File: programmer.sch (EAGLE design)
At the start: 16 parts, among them U1 ATMEGA8U2AU, Y1 16 MHz

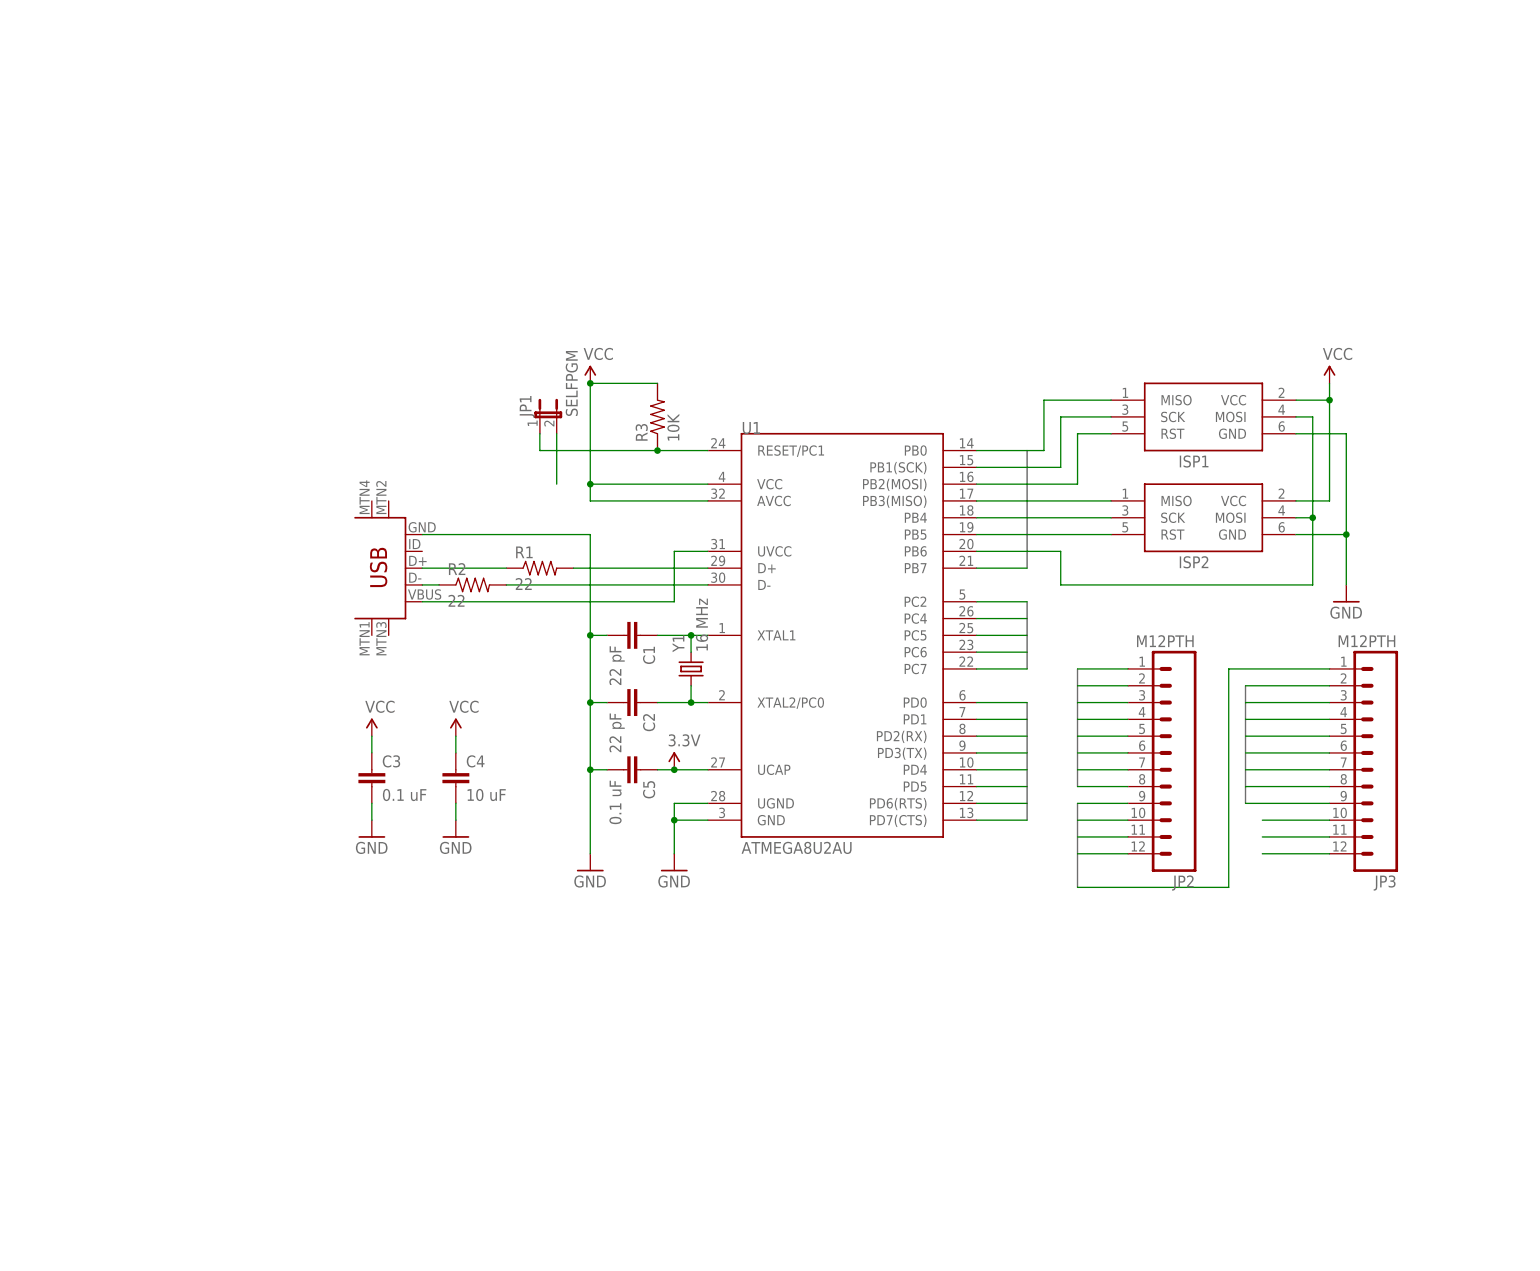
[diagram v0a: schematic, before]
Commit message: Angled 6-pin ISP.
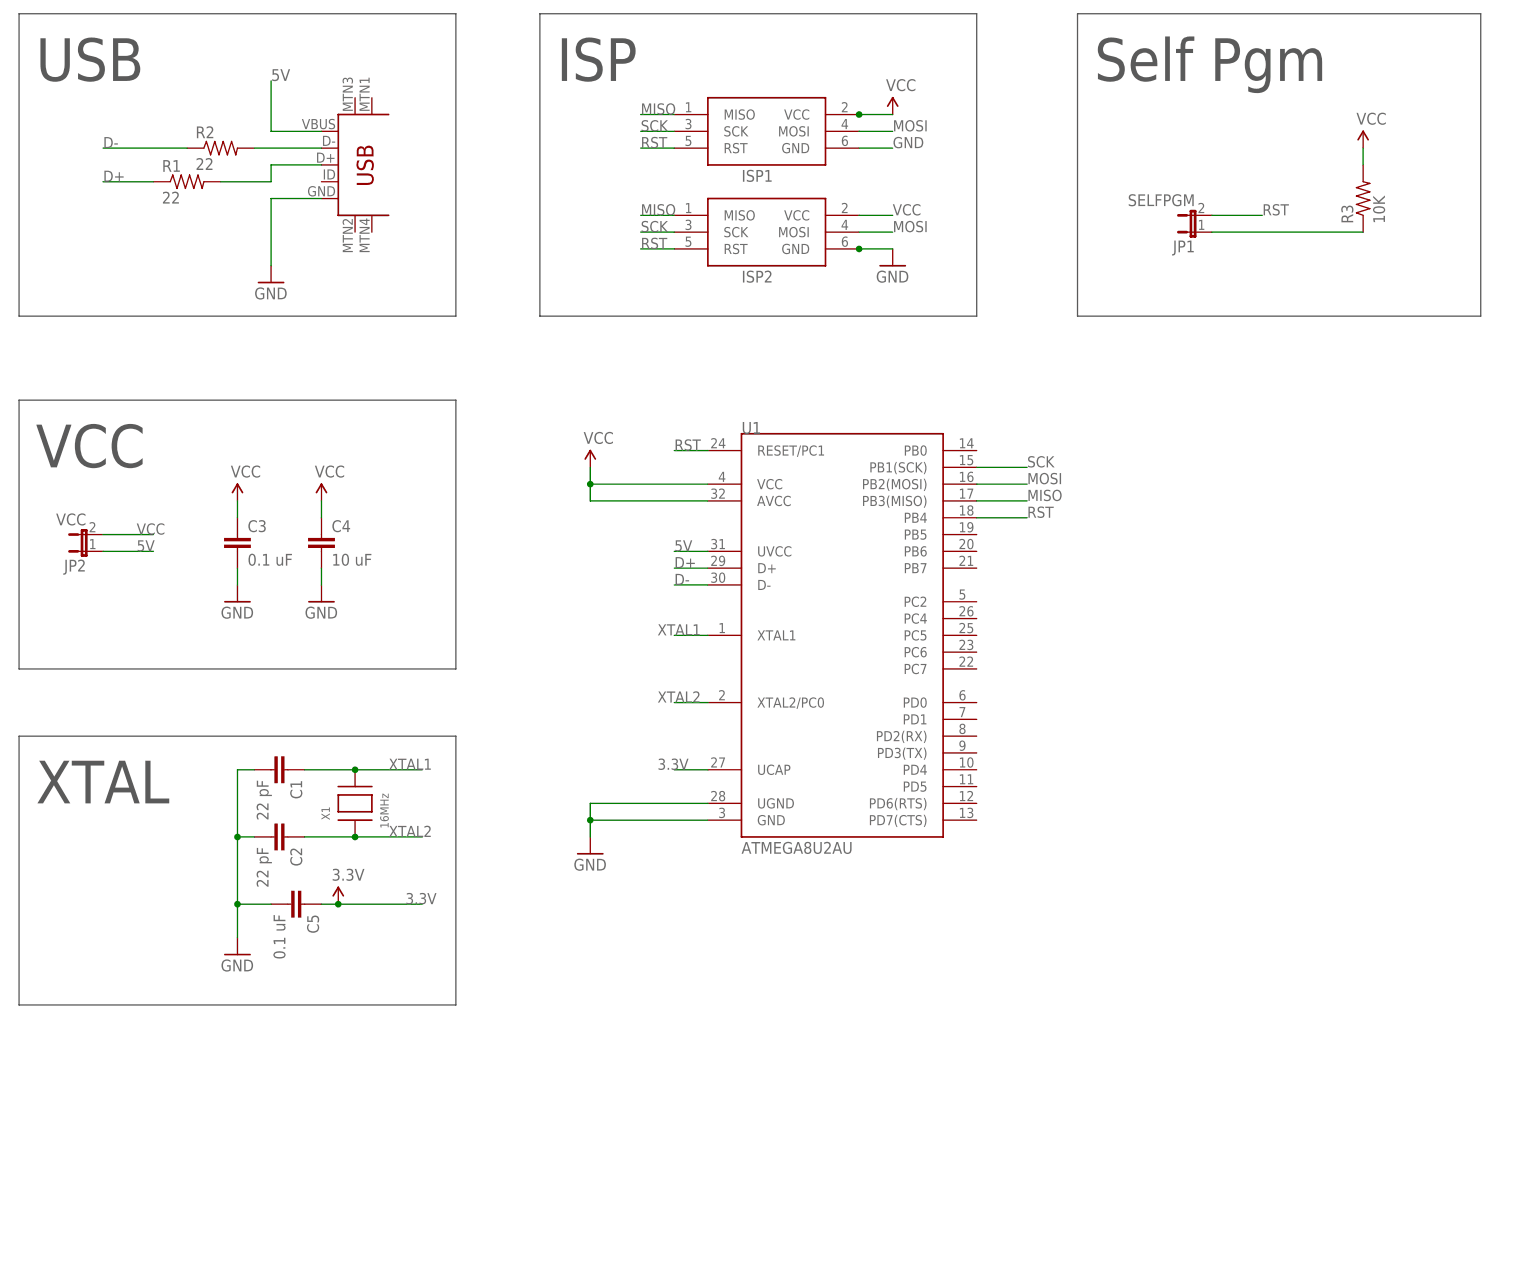
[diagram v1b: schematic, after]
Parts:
- removed JP3: M12PTH, SparkFun:M12PTH
- removed Y1: 16 MHz, SparkFun:CRYSTAL10.5X4.8
- added X1: 16MHz, adafruit:XTALNX8045
- JP2: value M12PTH -> VCC; device SparkFun:M12PTH -> SparkFun:JUMPER-2PTH
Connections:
- removed net D_MINUS: R2.1, U$1.D-
- removed net D_MINUS_MCU: R2.2, U1.D-
- removed net D_PLUS: R1.1, U$1.D+
- removed net D_PLUS_MCU: R1.2, U1.D+
- removed net N$5: U$1.VBUS, U1.UVCC
- removed net PB0: JP2.1, U1.PB0
- removed net PB1: ISP1.SCK, ISP2.SCK, JP2.2, U1.PB1(SCK)
- removed net PB2: ISP1.MOSI, ISP2.MOSI, JP2.3, U1.PB2(MOSI)
- removed net PB3: ISP1.MISO, ISP2.MISO, JP2.4, U1.PB3(MISO)
- removed net PB4: ISP1.RST, ISP2.RST, JP1.2, JP2.5, U1.PB4
- removed net PB5: JP2.6, U1.PB5
- removed net PB6: JP2.7, U1.PB6
- removed net PB7: JP2.8, U1.PB7
- removed net PC2: JP2.9, U1.PC2
- removed net PC4: JP2.10, U1.PC4
- removed net PC5: JP2.11, U1.PC5
- removed net PC6: JP2.12, U1.PC6
- removed net PC7: JP3.1, U1.PC7
- removed net PD0: JP3.2, U1.PD0
- removed net PD1: JP3.3, U1.PD1
- removed net PD2: JP3.4, U1.PD2(RX)
- removed net PD3: JP3.5, U1.PD3(TX)
- removed net PD4: JP3.6, U1.PD4
- removed net PD5: JP3.7, U1.PD5
- removed net PD6: JP3.8, U1.PD6(RTS)
- removed net PD7: JP3.9, U1.PD7(CTS)
- new net 5V: JP2.1, U$1.VBUS, U1.UVCC
- new net D+: R1.1, U1.D+
- new net D+RAW: R1.2, U$1.D+
- new net D-: R2.1, U1.D-
- new net MISO: ISP1.MISO, ISP2.MISO, U1.PB3(MISO)
- new net MOSI: ISP1.MOSI, ISP2.MOSI, U1.PB2(MOSI)
- new net N$2: R2.2, U$1.D-
- new net RST: ISP1.RST, ISP2.RST, JP1.2, U1.PB4, U1.RESET/PC1
- new net SCK: ISP1.SCK, ISP2.SCK, U1.PB1(SCK)
- net 3.3V: no longer JP3.10
- net GND: no longer JP3.12
- net RST_JP1: no longer U1.RESET/PC1
- net VCC: now also JP2.2; no longer JP3.11
- net XTAL1: now also X1.P$2; no longer Y1.2
- net XTAL2: now also X1.P$1; no longer Y1.1
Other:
- note added: "ISP"
- note added: "Self Pgm"
- note added: "USB"
- note added: "VCC"
- note added: "XTAL"
- moved on the sheet: C1, C2, C3, C4, C5, ISP1, ISP2, JP1, R1, R2, R3

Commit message: Blinkenlights.
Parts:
- added LED1, LED2: (no value), adafruit:LEDSMT1206
- added R4, R5: 1K, SparkFun:RESISTOR0805-RES
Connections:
- new net LED_ACTIVE: LED2.C, U1.PD1
- new net LED_WRITE: LED1.C, U1.PD0
- new net N$1: LED2.A, R5.1
- new net N$3: LED1.A, R4.1
- net VCC: now also R4.2, R5.2
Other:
- note added: "LED"
- moved on the sheet: U1

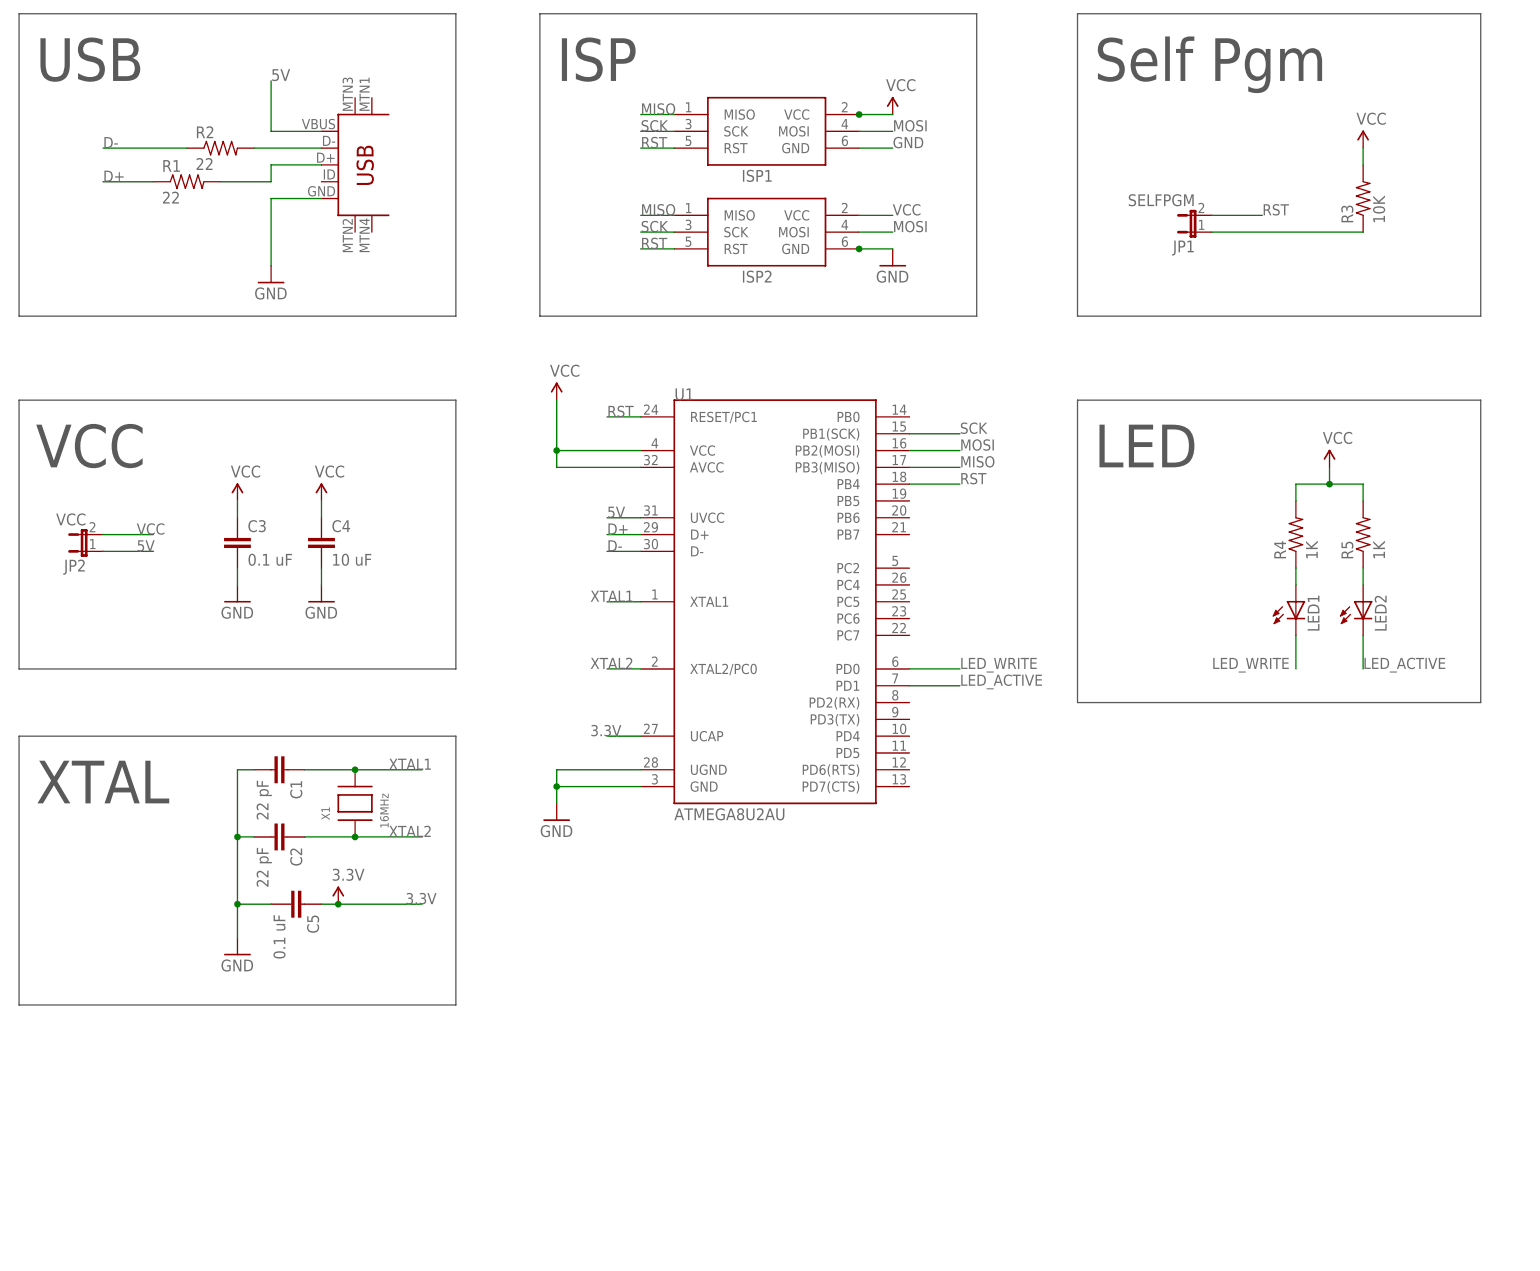
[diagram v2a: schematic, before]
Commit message: More work on layout. SJ1. Polarized 10uF cap. Fixed ISP2 orientation.
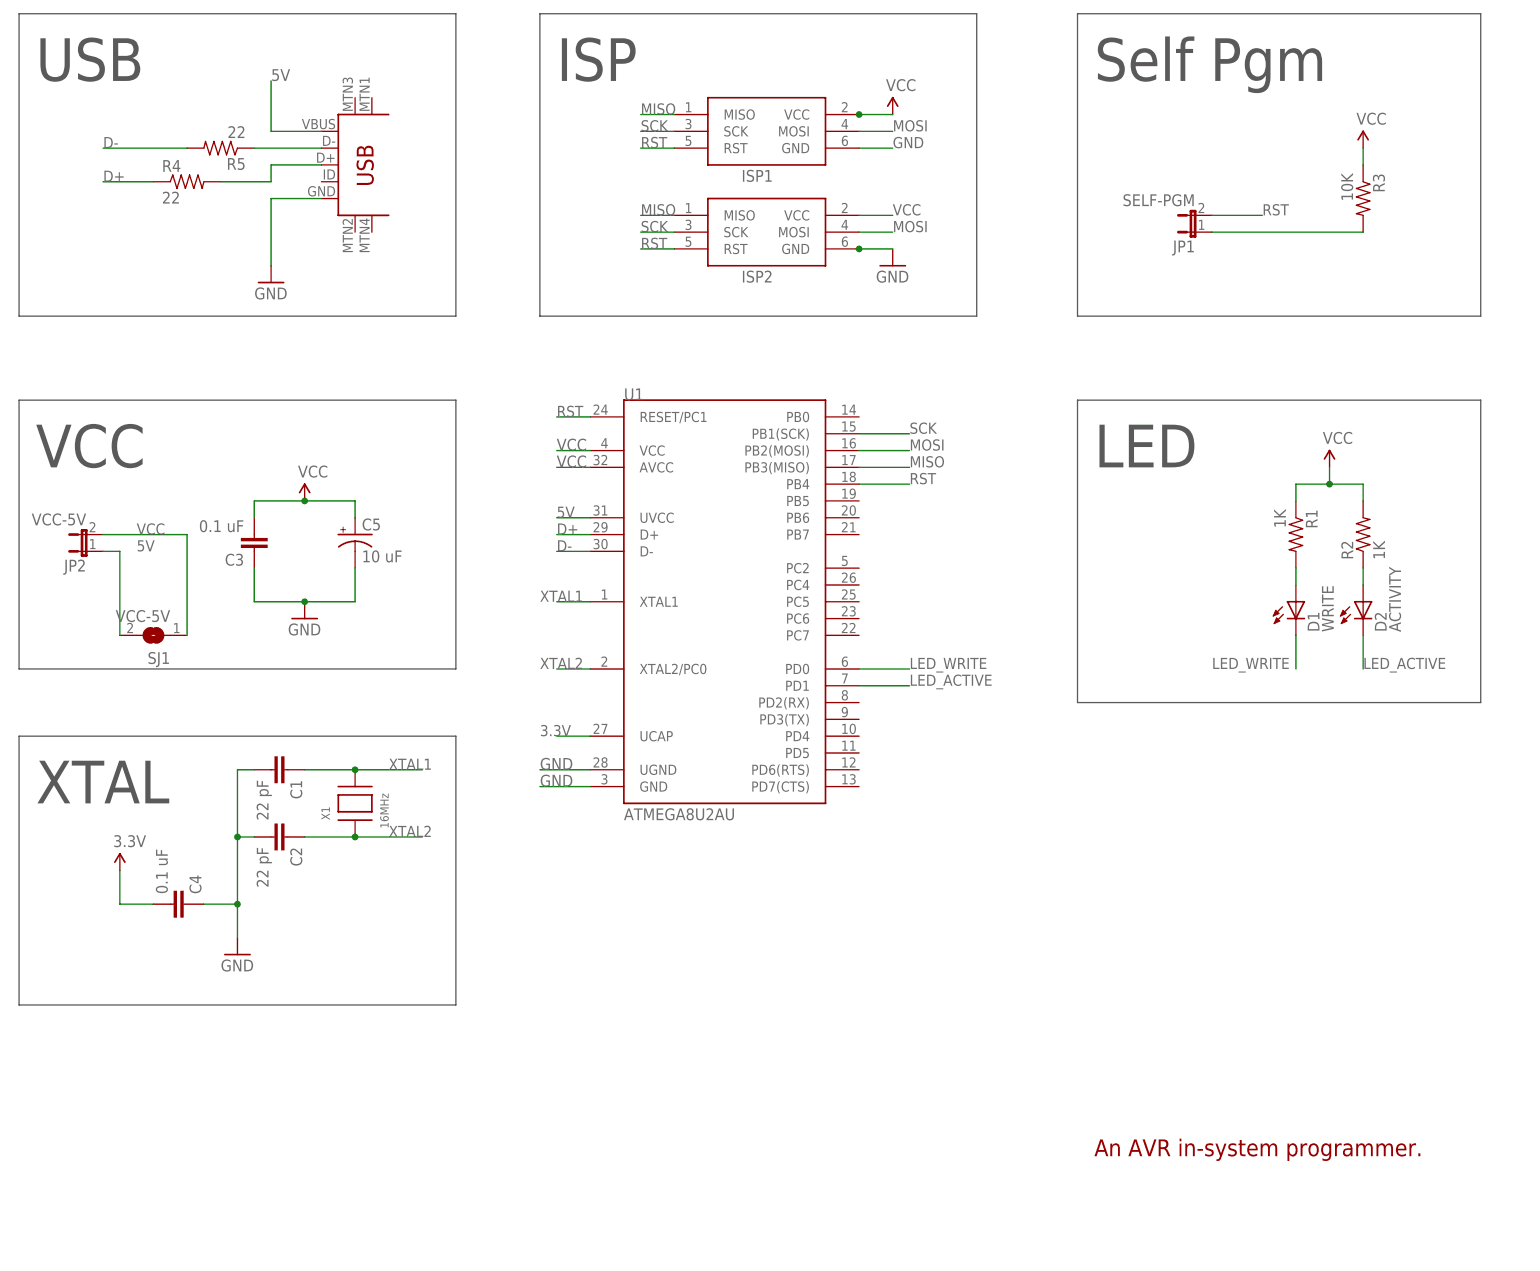
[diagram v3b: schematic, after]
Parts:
- added SJ1: VCC-5V, jumper:SJ
- C4: value 10 uF -> 0.1 uF
- C5: value 0.1 uF -> 10 uF; device SparkFun:CAP0805 -> SparkFun:CAP_POL1206
- D1: value (none) -> WRITE
- D2: value (none) -> ACTIVITY
- JP1: value SELFPGM -> SELF-PGM
- JP2: value VCC -> VCC-5V
- R1, R2: value 22 -> 1K
- R4, R5: value 1K -> 22
- renumbered LED1 to D1, LED2 to D2, U$1 to USB
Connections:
- net 3.3V: now also C4.2; no longer C5.1
- net 5V: now also SJ1.2
- net D+: now also R4.1; no longer R1.1
- net D+RAW: now also R4.2; no longer R1.2
- net D-: now also R5.2; no longer R2.1
- net GND: now also C3.1, C4.1, C5.-; no longer C3.2, C4.2, C5.2
- net N$1: now also R2.1; no longer R5.1
- net N$2: now also R5.1; no longer R2.2
- net N$3: now also R1.2; no longer R4.1
- net RST_JP1: now also R3.2; no longer R3.1
- net VCC: now also C3.2, C5.+, R1.1, R2.2, R3.1, SJ1.1; no longer C3.1, C4.1, R3.2, R4.2, R5.2
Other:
- note added: "An AVR in-system programmer."
- moved on the sheet: C3, C4, R1, R2, R3, R4, R5, U1

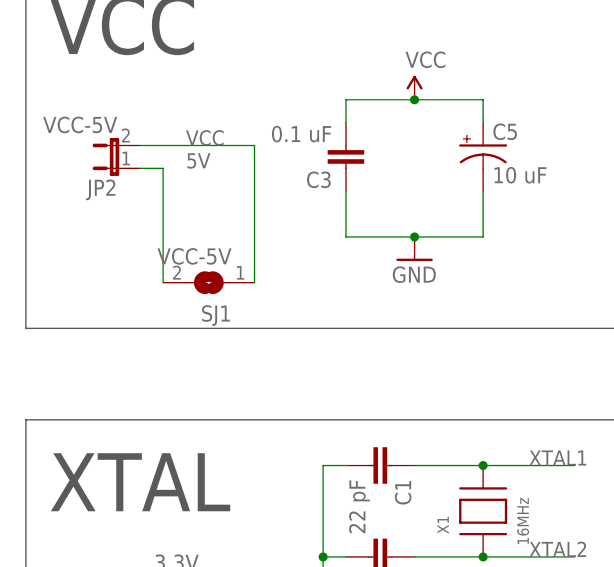
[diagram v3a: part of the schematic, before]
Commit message: Better routing setup. Moved SJ1 jumper temporarily.
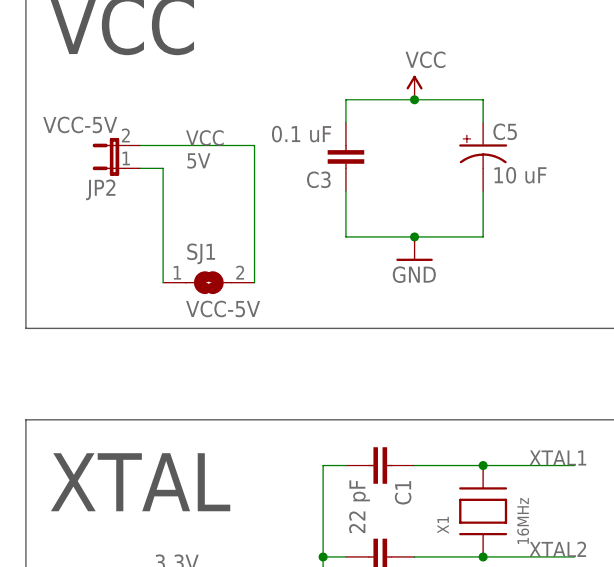
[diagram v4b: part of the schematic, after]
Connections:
- net 5V: now also SJ1.1; no longer SJ1.2
- net VCC: now also SJ1.2; no longer SJ1.1
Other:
- moved on the sheet: SJ1
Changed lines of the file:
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@@
 <instance part="R2" gate="G$1" x="142.24" y="60.96" rot="R90"/>
 <instance part="P+7" gate="1" x="137.16" y="71.12"/>
-<instance part="SJ1" gate="1" x="-40.64" y="45.72" rot="R180"/>
+<instance part="SJ1" gate="1" x="-40.64" y="45.72"/>
 <instance part="C5" gate="G$1" x="-10.16" y="60.96"/>
 </instances>
@@
 <wire x1="-48.26" y1="60.96" x2="-35.56" y2="60.96" width="0.1524" layer="91"/>
 <label x="-43.18" y="60.96" size="1.6764" layer="95" font="vector"/>
-<pinref part="SJ1" gate="1" pin="1"/>
+<pinref part="SJ1" gate="1" pin="2"/>
 <wire x1="-35.56" y1="60.96" x2="-35.56" y2="45.72" width="0.1524" layer="91"/>
 </segment>
@@
 <label x="-43.18" y="58.42" size="1.6764" layer="95" font="vector"/>
 <wire x1="-45.72" y1="58.42" x2="-45.72" y2="45.72" width="0.1524" layer="91"/>
-<pinref part="SJ1" gate="1" pin="2"/>
-</segment>
-</net>
+<pinref part="SJ1" gate="1" pin="1"/>
+</segment>
+</net>
